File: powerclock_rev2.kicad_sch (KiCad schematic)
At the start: 76 parts, among them J1 IN HEAD2, J10 LED OUT HEAD1, J11 LED OUT SOCK1, J12 CLK OUT, J13 /4 OUT, J14 /16 OUT, J15 /64 OUT, J16 JACK OUT SOCK, J17 /2 OUT, J18 /8 OUT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

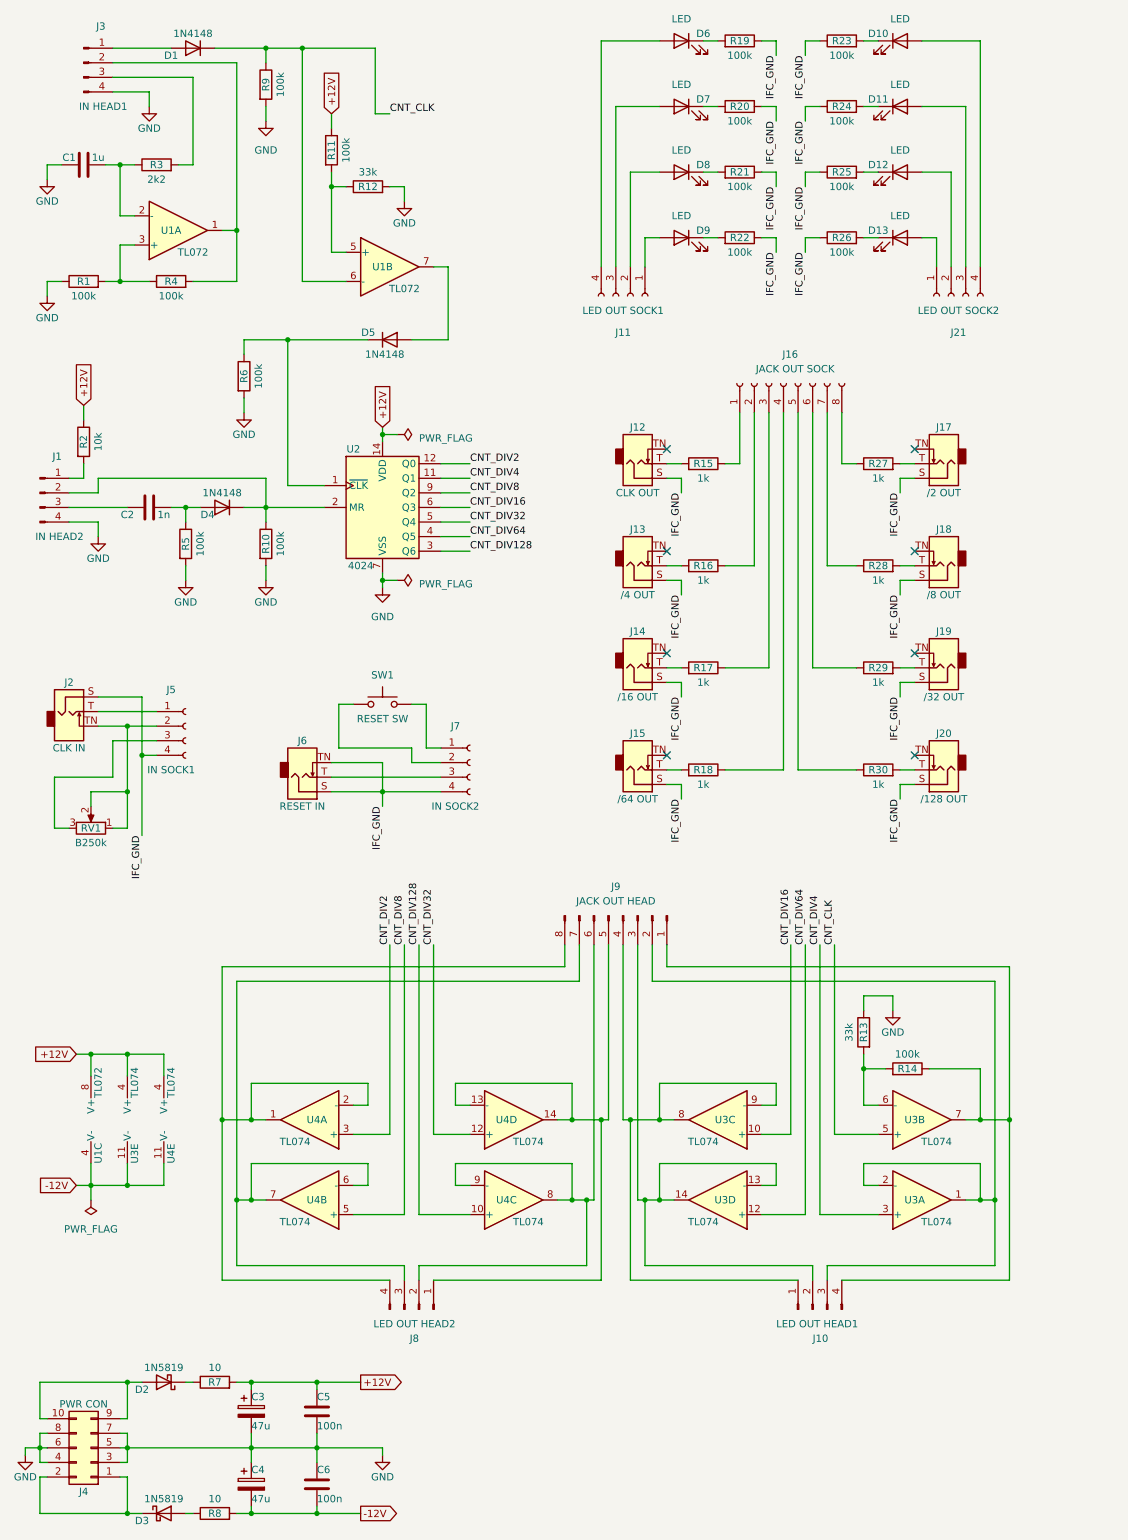
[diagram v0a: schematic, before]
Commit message: Add license disclaimers
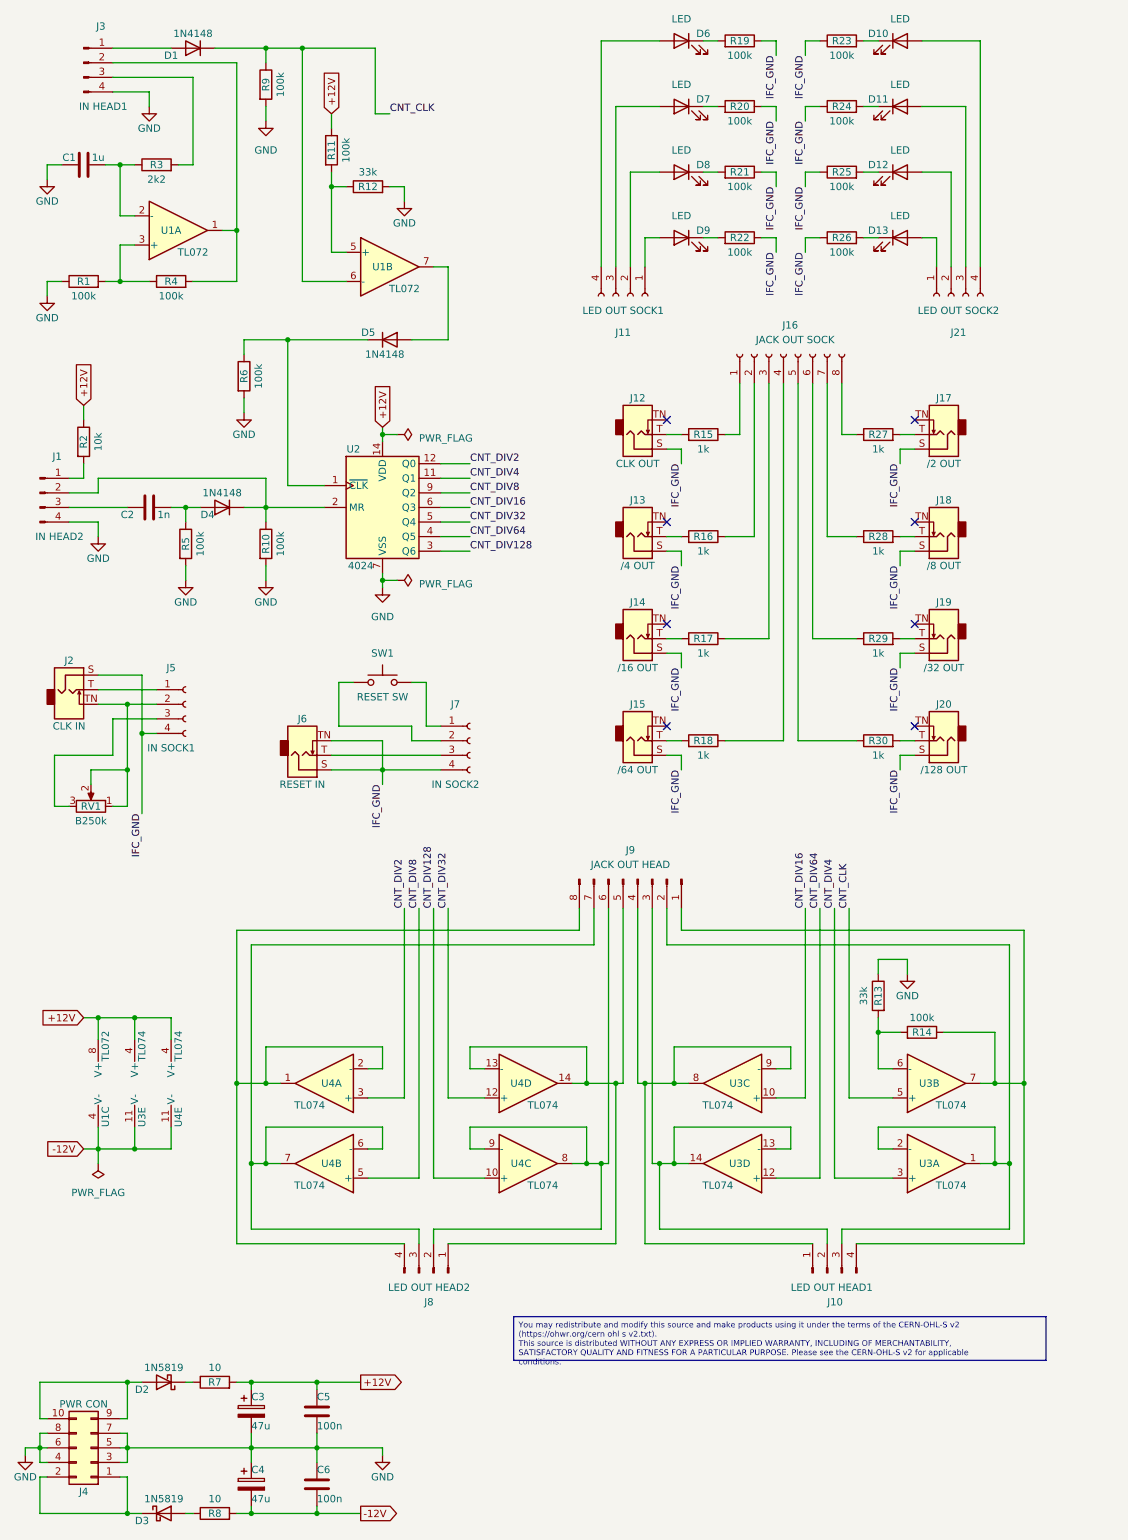
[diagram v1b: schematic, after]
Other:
- moved on the sheet: J10, J12, J13, J14, J15, J16, J17, J18, J19, J2, J20, J5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
